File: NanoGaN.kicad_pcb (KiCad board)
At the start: 6 copper layers, 60 x 100 mm, 190 parts, among them J1 XT60-M, J10 Conn_01x06, J11 Conn_01x04, J12 USB_C_Receptacle_USB2.0_16P, J14 Conn_01x03, J2 XT60-M, J3 Phase_U, J4 Phase_V, J5 Phase_W, J6 FTSH-107-01-L-DV-K-TR, J7 Conn_01x03, J8 Conn_01x02, J9 Conn_01x07, Q1 IGC025S08S1, Q2 IGC025S08S1, Q3 IGC025S08S1, Q4 IGC025S08S1, Q5 IGC025S08S1, Q6 IGC025S08S1, Q7 Si2302CDS, U1 STM32H723VGTx, U12 LMG1205YFXR, U13 BMI323, U14 AS5047P-ATST, U15 TCAN1044VDRQ1, U2 LMR51635XDDCR, U3 AMS1117, U4 ACS37030LLZATR-065B3, U5 LMG1205YFXR, U6 ACS37030LLZATR-065B3, U7 ACS37030LLZATR-065B3, U8 LMG1205YFXR, X1 8MHz

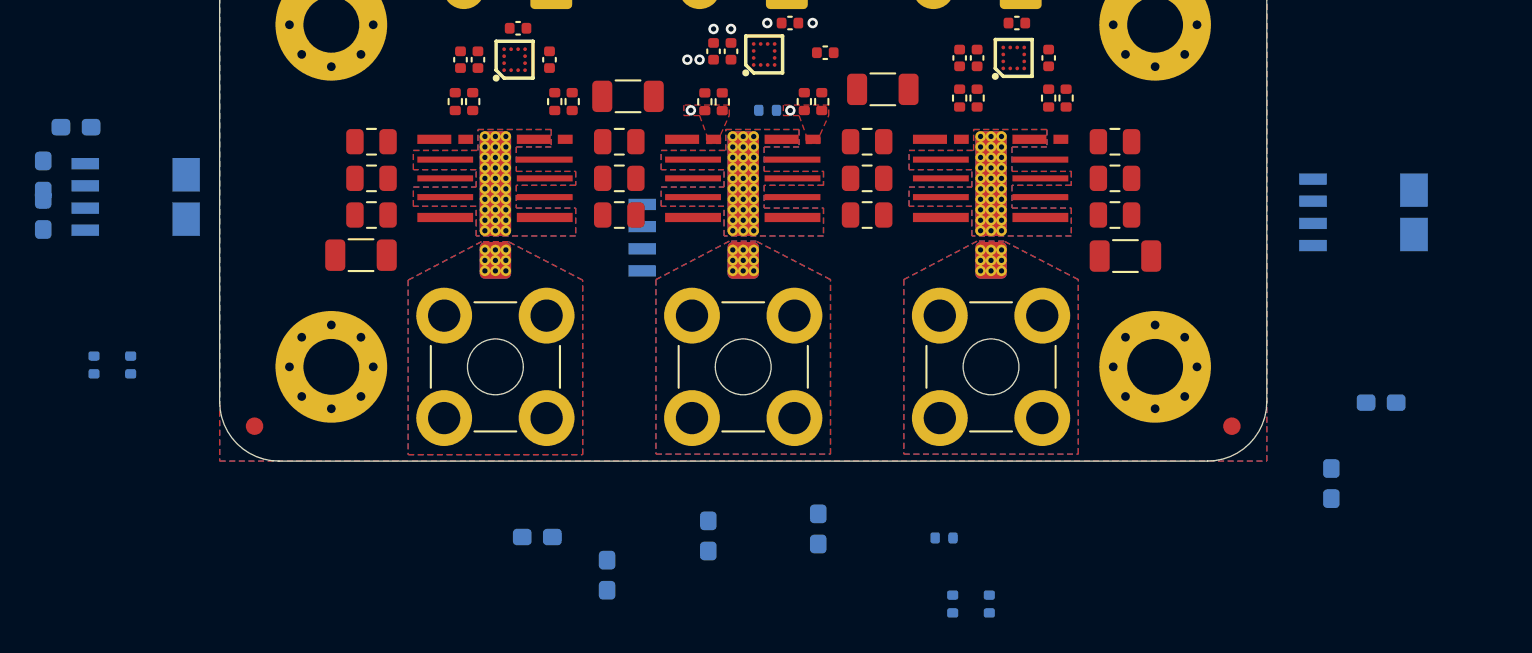
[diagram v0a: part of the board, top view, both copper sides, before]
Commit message: placed a few back side components
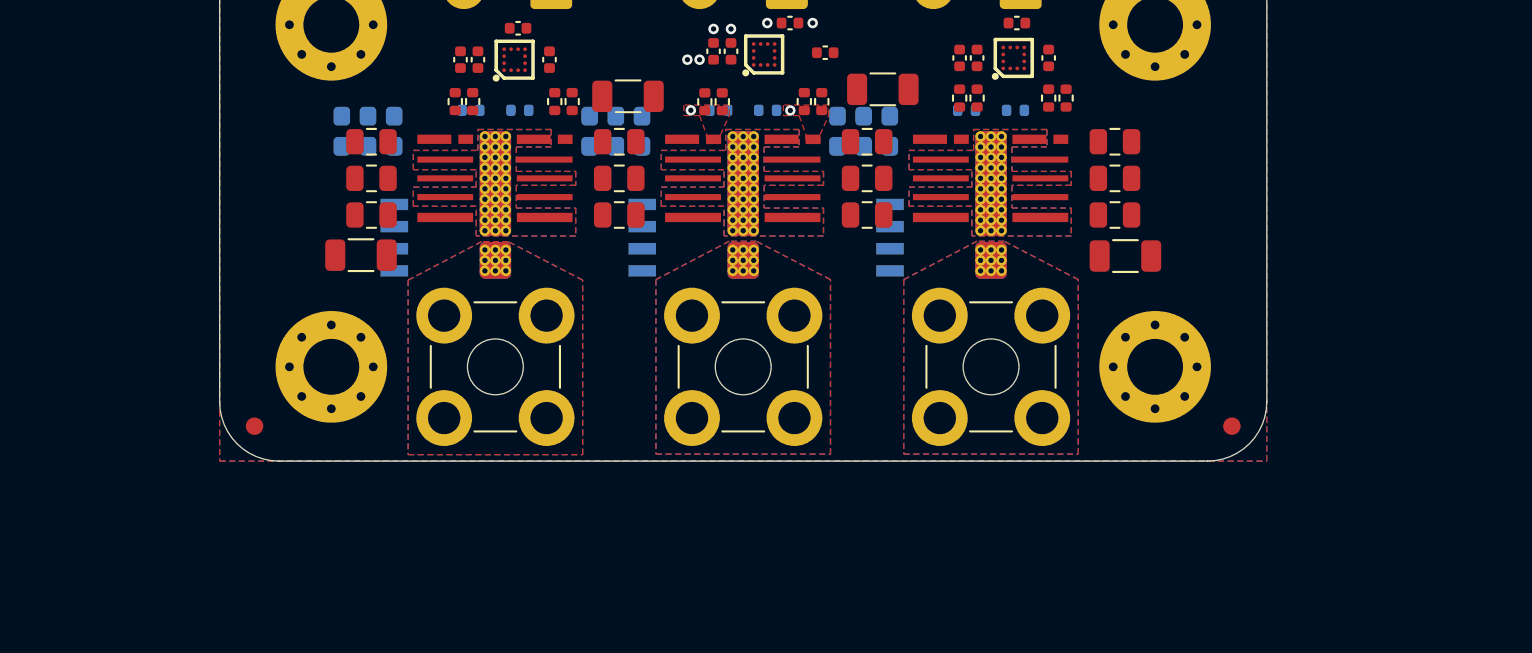
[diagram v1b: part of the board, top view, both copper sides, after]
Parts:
- moved C28 33.6 mm to (152.1, 129.1)
- moved C24 32.2 mm to (153.6, 129.1), turned to 90 degrees
- moved R13 28.3 mm to (160.8, 127.9), turned to 180 degrees
- moved R14 28.3 mm to (158.0, 127.9), turned to 0 degrees
- moved R18 27.7 mm to (143.8, 127.9)
- moved R24 26.6 mm to (132.4, 127.9), turned to 180 degrees
- moved R25 26.1 mm to (129.6, 127.9), turned to 0 degrees
- moved C39 25.4 mm to (137.9, 129.1)
- moved U4 24.3 mm to (156.5, 135.2)
- moved C26 24.2 mm to (136.4, 129.1), turned to 90 degrees
- moved C38 24.0 mm to (139.4, 129.1), turned to 90 degrees
- moved C25 22.8 mm to (150.6, 129.1), turned to 90 degrees
- moved C91 18.8 mm to (123.7, 129.1)
- moved C89 18.2 mm to (125.2, 129.1), turned to 90 degrees
- moved U7 17.9 mm to (128.1, 135.2)
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
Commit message: wip layout
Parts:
- moved C18 4.59 mm to (151.8, 115.3), turned to -90 degrees
- moved R5 2.60 mm to (153.5, 115.2), turned to -90 degrees
- moved C87 2.20 mm to (159.9, 112.2)
- moved R10 2.20 mm to (160.4, 115.2)
- moved R12 2.20 mm to (159.9, 113.2)
- moved C34 1.20 mm to (148.7, 124.5), turned to 90 degrees
- moved C17 0.50 mm to (139.0, 126.8)
- moved C42 0.10 mm to (153.2, 126.8)
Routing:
- net GND: vias 45 -> 50

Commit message: wip layout
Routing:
- net GND: vias 50 -> 65
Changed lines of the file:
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@@
+	)
+	(via
+		(at 141.2651 128.2)
+		(size 0.6)
+		(drill 0.3)
+		(layers "F.Cu" "B.Cu")
+		(net 3)
 	)
 	(via
@@
 	)
 	(via
+		(at 141.5651 135.5)
+		(size 0.6)
+		(drill 0.3)
+		(layers "F.Cu" "B.Cu")
+		(net 3)
+	)
+	(via
 		(at 140.9651 92.8)
 		(size 0.6)
@@
 	)
 	(via
+		(at 140.6651 128.2)
+		(size 0.6)
+		(drill 0.3)
+		(layers "F.Cu" "B.Cu")
+		(net 3)
+	)
+	(via
 		(at 149.6651 59.2)
 		(size 0.6)
@@
 	)
 	(via
+		(at 140.6651 125)
+		(size 0.6)
+		(drill 0.3)
+		(layers "F.Cu" "B.Cu")
+		(net 3)
+	)
+	(via
 		(at 120.7651 78.8)
 		(size 0.6)
@@
 	)
 	(via
+		(at 140.0651 125)
+		(size 0.6)
+		(drill 0.3)
+		(layers "F.Cu" "B.Cu")
+		(net 3)
+	)
+	(via
+		(at 138.8651 128.2)
+		(size 0.6)
+		(drill 0.3)
+		(layers "F.Cu" "B.Cu")
+		(net 3)
+	)
+	(via
+		(at 140.9651 135.5)
+		(size 0.6)
+		(drill 0.3)
+		(layers "F.Cu" "B.Cu")
+		(net 3)
+	)
+	(via
 		(at 160.9651 100.4)
 		(size 0.6)
@@
 	)
 	(via
+		(at 140.0651 128.2)
+		(size 0.6)
+		(drill 0.3)
+		(layers "F.Cu" "B.Cu")
+		(net 3)
+	)
+	(via
+		(at 139.4651 128.2)
+		(size 0.6)
+		(drill 0.3)
+		(layers "F.Cu" "B.Cu")
+		(net 3)
+	)
+	(via
 		(at 128.3851 91)
 		(size 0.6)
@@
 	)
 	(via
+		(at 141.2651 128.8)
+		(size 0.6)
+		(drill 0.3)
+		(layers "F.Cu" "B.Cu")
+		(net 3)
+	)
+	(via
 		(at 134.0651 76.3)
 		(size 0.6)
@@
 	)
 	(via
+		(at 141.2651 125)
+		(size 0.6)
+		(drill 0.3)
+		(layers "F.Cu" "B.Cu")
+		(net 3)
+	)
+	(via
 		(at 151.2651 87.8)
 		(size 0.6)
@@
 	)
 	(via
+		(at 140.0651 128.8)
+		(size 0.6)
+		(drill 0.3)
+		(layers "F.Cu" "B.Cu")
+		(net 3)
+	)
+	(via
 		(at 137.8651 92.9)
 		(size 0.6)
@@
 	)
 	(via
+		(at 139.4651 125)
+		(size 0.6)
+		(drill 0.3)
+		(layers "F.Cu" "B.Cu")
+		(net 3)
+	)
+	(via
+		(at 141.8651 125)
+		(size 0.6)
+		(drill 0.3)
+		(layers "F.Cu" "B.Cu")
+		(net 3)
+	)
+	(via
 		(at 158.6651 100.4)
 		(size 0.6)
@@
 	)
 	(via
+		(at 142.4651 125)
+		(size 0.6)
+		(drill 0.3)
+		(layers "F.Cu" "B.Cu")
+		(net 3)
+	)
+	(via
 		(at 143.3651 134.9)
 		(size 0.6)
@@
 	)
 	(via
+		(at 140.6651 128.8)
+		(size 0.6)
+		(drill 0.3)
+		(layers "F.Cu" "B.Cu")
+		(net 3)
+	)
+	(via
 		(at 152.1651 85.25)
 		(size 0.6)
@@
 	)
 	(via
-		(at 142.6651 125)
+		(at 142.1651 135.5)
 		(size 0.6)
 		(drill 0.3)
@@
 		(size 0.6)
 		(drill 0.3)
-		(layers "F.Cu" "B.Cu")
-		(net 3)
-	)
-	(via
-		(at 141.9651 125)
-		(size 0.6)
-		(drill 0.3)

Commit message: cooling once again
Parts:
- moved HS1 14.3 mm to (245.2, 131.8)
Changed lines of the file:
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@@
 		(tenting front back)
 		(aux_axis_origin 115.1651 148)
-		(grid_origin 145.1651 142.6)
+		(grid_origin 145.1651 75)
 		(pcbplotparams
 			(layerselection 0x00000000_00000000_55555555_5755f5ff)
@@
 	(footprint "NanoGaN:ICK_S"
 		(layer "F.Cu")
-		(at 259.3651 133)
+		(at 245.1651 131.8)
 		(property "Reference" "HS1"
 			(at 0 -0.5 0)
@@
 		(model "${KIPRJMOD}/NanoGaN_3D_models/ICK_S.step"
 			(offset
-				(xyz -22.5 -3.75 1.1)
+				(xyz -22.5 -3.75 1.5)
 			)
 			(scale
@@
 		)
 		(embedded_fonts no)
-		(model "${KIPRJMOD}/NanoGaN_3D_models/cc_v4.step"
+		(model "${KIPRJMOD}/NanoGaN_3D_models/cc_v5.step"
 			(offset
-				(xyz -23.5 23.5 -0.5)
+				(xyz 0 0 0)
 			)
 			(scale

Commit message: wip layout
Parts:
- moved C36 23.1 mm to (153.3, 123.2), turned to 90 degrees
- moved R20 21.8 mm to (152.1, 123.5), turned to 90 degrees
- moved R19 19.2 mm to (150.9, 123.2)
- moved C25 16.9 mm to (166.9, 133.6)
- moved C33 16.9 mm to (138.5, 133.6)
- moved C26 16.9 mm to (152.7, 133.6)
- moved C28 16.7 mm to (166.9, 136.8), turned to -90 degrees
- moved C91 16.7 mm to (138.5, 136.8), turned to -90 degrees
- moved C39 16.7 mm to (152.7, 136.8), turned to -90 degrees
- moved C89 16.0 mm to (137.0, 139.9), turned to -90 degrees
- moved C38 16.0 mm to (151.2, 139.9), turned to -90 degrees
- moved C24 15.9 mm to (165.3, 139.9), turned to -90 degrees
- moved C7 12.3 mm to (133.0, 96.2), turned to -90 degrees
- moved C79 12.3 mm to (134.0, 96.2), turned to -90 degrees
- moved C8 7.21 mm to (130.2, 83.8), turned to 90 degrees
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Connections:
- C25 pad 1: /HalfBridgeU/I_CURR_SENS- -> /HalfBridgeU/I_CURR_SENS+
- C26 pad 1: /HalfBridgeV/I_CURR_SENS- -> /HalfBridgeV/I_CURR_SENS+
- C28 pad 1: /HalfBridgeU/I_CURR_SENS+ -> /HalfBridgeU/I_CURR_SENS-
- C33 pad 1: /HalfBridgeW/I_CURR_SENS- -> /HalfBridgeW/I_CURR_SENS+
- C39 pad 1: /HalfBridgeV/I_CURR_SENS+ -> /HalfBridgeV/I_CURR_SENS-
- C91 pad 1: /HalfBridgeW/I_CURR_SENS+ -> /HalfBridgeW/I_CURR_SENS-
- U1 pad 30: /HalfBridgeU/I_CURR_SENS+ -> /HalfBridgeW/I_CURR_SENS+
- U1 pad 31: /HalfBridgeU/I_CURR_SENS- -> /HalfBridgeW/I_CURR_SENS-
- U1 pad 34: /HalfBridgeW/I_CURR_SENS- -> /HalfBridgeU/I_CURR_SENS+
- U1 pad 35: /HalfBridgeW/I_CURR_SENS+ -> /HalfBridgeU/I_CURR_SENS-
- U4 pad 1: /HalfBridgeU/HS -> /HalfBridgeU/PHASE
- U4 pad 2: /HalfBridgeU/PHASE -> /HalfBridgeU/HS
- U4 pad 4: /HalfBridgeU/I_CURR_SENS- -> /HalfBridgeU/I_CURR_SENS+
- U4 pad 5: /HalfBridgeU/I_CURR_SENS+ -> /HalfBridgeU/I_CURR_SENS-
- U6 pad 1: /HalfBridgeV/HS -> /HalfBridgeV/PHASE
- U6 pad 2: /HalfBridgeV/PHASE -> /HalfBridgeV/HS
- U6 pad 4: /HalfBridgeV/I_CURR_SENS- -> /HalfBridgeV/I_CURR_SENS+
- U6 pad 5: /HalfBridgeV/I_CURR_SENS+ -> /HalfBridgeV/I_CURR_SENS-
- U7 pad 1: /HalfBridgeW/HS -> /HalfBridgeW/PHASE
- U7 pad 2: /HalfBridgeW/PHASE -> /HalfBridgeW/HS
- U7 pad 4: /HalfBridgeW/I_CURR_SENS- -> /HalfBridgeW/I_CURR_SENS+
- U7 pad 5: /HalfBridgeW/I_CURR_SENS+ -> /HalfBridgeW/I_CURR_SENS-
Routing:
- net /HalfBridgeU/I_CURR_SENS-: track 0.00 -> 69.0 mm, vias 0 -> 1
- net /HalfBridgeU/I_CURR_SENS+: track 0.00 -> 67.7 mm, vias 0 -> 1
- net /HalfBridgeV/I_CURR_SENS-: track 0.00 -> 64.7 mm, vias 0 -> 1
- net /HalfBridgeV/I_CURR_SENS+: track 0.00 -> 63.5 mm, vias 0 -> 1
- net /HalfBridgeW/I_CURR_SENS-: track 0.00 -> 59.1 mm, vias 0 -> 1
- net /HalfBridgeW/I_CURR_SENS+: track 0.00 -> 58.1 mm, vias 0 -> 1
- net /HalfBridgeV/GATE+: track 0.00 -> 44.6 mm
- net /HalfBridgeV/GATE-: track 0.00 -> 44.5 mm
- net /HalfBridgeV/HS: track 0.00 -> 15.2 mm, vias 0 -> 1
- net GND: track 0.89 -> 15.1 mm, vias 65 -> 88
- net +5V: track 0.89 -> 7.01 mm
- net +3V3: track 0.00 -> 6.02 mm, vias 16 -> 19
- net /HalfBridgeV/HOH: track 0.00 -> 3.68 mm
- net /HalfBridgeV/LOL: track 0.00 -> 3.62 mm
- net /HalfBridgeV/LOH: track 0.00 -> 3.16 mm
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
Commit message: wip layout
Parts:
- moved C36 31.9 mm to (184.9, 118.9)
- moved R19 31.9 mm to (182.5, 118.9)
- moved R20 31.9 mm to (183.7, 119.2)
- moved C18 31.6 mm to (183.4, 114.5)
- moved R4 31.6 mm to (186.4, 114.5)
- moved R5 31.6 mm to (185.1, 114.4)
- moved C87 23.7 mm to (182.7, 105.7)
- moved R10 23.7 mm to (183.2, 108.7)
- moved R12 23.7 mm to (182.7, 106.7)
- moved C48 1.43 mm to (133.7, 122.9), turned to 0 degrees
- moved C6 1.26 mm to (156.9, 90.1)
- moved C82 1.26 mm to (154.4, 90.1)
- moved C86 1.26 mm to (151.9, 90.1)
- moved R2 1.26 mm to (151.5, 104.3)
- moved C5 1.26 mm to (151.5, 101.5)
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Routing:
- net /HalfBridgeW/GATE+: track 0.00 -> 47.3 mm
- net /HalfBridgeW/GATE-: track 0.00 -> 47.2 mm
- net /HalfBridgeU/GATE+: track 0.00 -> 47.2 mm
- net /HalfBridgeU/GATE-: track 0.00 -> 47.1 mm
- net +5V: track 7.01 -> 17.6 mm, vias 19 -> 26
- net /HalfBridgeU/HS: track 0.00 -> 7.99 mm, vias 0 -> 1
- net /HalfBridgeW/HS: track 0.00 -> 7.98 mm, vias 0 -> 1
- net /HalfBridgeW/HOH: track 0.00 -> 3.68 mm
- net /HalfBridgeU/HOH: track 0.00 -> 3.68 mm
- net /HalfBridgeW/LOL: track 0.00 -> 3.62 mm
- net /HalfBridgeU/LOL: track 0.00 -> 3.62 mm
- net /HalfBridgeW/LOH: track 0.00 -> 3.16 mm
- net /HalfBridgeU/LOH: track 0.00 -> 3.16 mm
- net /HalfBridgeW/HOL: track 0.00 -> 2.76 mm
- net /HalfBridgeU/HOL: track 0.00 -> 2.76 mm
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- added copper zone on F.Cu, net /HalfBridgeU/HIGH_GATE
- added copper zone on F.Cu, net /HalfBridgeU/LOW_GATE
- added copper zone on F.Cu, net /HalfBridgeW/HIGH_GATE
- added copper zone on F.Cu, net /HalfBridgeW/LOW_GATE
